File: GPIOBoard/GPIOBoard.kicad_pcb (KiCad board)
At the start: 2 copper layers, 70 x 45 mm, 85 parts, among them J1 GPIO1, J10 USB_C_Receptacle_USB2.0_16P, J11 SWD, J12 CAN, J2 GPIO2, J3 GPIO3, J4 GPIO4, J5 GPIO5, J6 GPIO6, J7 GPIO7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

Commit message: GPIO Board ver1.1
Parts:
- removed the REF** at (156.2, 99.9)
- added D17: CAN_R, LED_SMD:LED_0603_1608Metric, F.Cu at (132.2, 94.5)
- added R27: 420, Resistor_SMD:R_0603_1608Metric, F.Cu at (128.6, 94.5)
- added R28: 100, Resistor_SMD:R_0603_1608Metric, F.Cu at (162.5, 90.8)
- added R29: 600, Resistor_SMD:R_0603_1608Metric, F.Cu at (162.5, 92.5)
- added R30: 300, Resistor_SMD:R_0603_1608Metric, F.Cu at (162.5, 94.2)
- added R31: 10k, Resistor_SMD:R_0603_1608Metric, F.Cu at (142.7, 97.5)
- added REF**: Title, Anan-Robo_Footprint_Library:Title, F.Cu at (167.9, 113.6)
- added REF**: Info_M, Anan-Robo_Footprint_Library:Info_M, B.Cu at (156.2, 100.4)
- added U5: LED_GRB, LED_SMD:LED_ROHM_SMLVN6, F.Cu at (169.2, 106.0)
- C1, C2: value 10u -> 4.7u
- D11: value 3V3 -> PWR
- D12: value data -> Data
- D15, D16: footprint Diode_SMD:D_SOD-123 -> Diode_SMD:Nexperia_CFP3_SOD-123W
- J10: value USB_C_Receptacle_USB2.0_16P -> Debug
- R17, R18, R20, R23, R24: value 55 -> 96
- R19: value 150 -> 430
- SW3: footprint Anan-Robo_Footprint_Library:SSSS213202 -> Anan-Robo_Footprint_Library:SLW
- U2: value LM1117GS -> TLV1117-33
- moved D11 40.4 mm to (135.5, 108.8), turned to 0 degrees
- moved R19 37.1 mm to (135.5, 106.8), turned to 0 degrees
- moved C1 4.72 mm to (138.8, 104.2)
- moved C2 4.72 mm to (138.8, 101.0)
- moved SW3 4.08 mm to (134.5, 89.2)
- moved D16 3.50 mm to (122.8, 103.0)
- moved R25 3.27 mm to (134.6, 97.0)
- moved C12 3.25 mm to (135.2, 101.5)
- moved U2 3.18 mm to (144.5, 103.2)
- moved U4 3.17 mm to (130.5, 101.5)
- moved JP1 3.07 mm to (128.6, 97.0)
- moved F1 2.25 mm to (122.0, 101.8)
- moved Y1 1.64 mm to (153.4, 91.7)
- moved C10 1.23 mm to (157.1, 90.8)
- moved C9 1.23 mm to (157.1, 92.8)
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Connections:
- U1 pad 10: unconnected-(U1-PA4-Pad10) -> /MCU/LED_R
- U1 pad 18: unconnected-(U1-PA8-Pad18) -> /MCU/LED_G
- U1 pad 6: unconnected-(U1-PA0-Pad6) -> /MCU/LED_B
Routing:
- net /MCU/LED_G: track 0.00 -> 22.9 mm, vias 0 -> 2
- net /MCU/LED_R: track 0.00 -> 17.6 mm, vias 0 -> 2
- net Net-(R28-Pad1): track 0.00 -> 16.5 mm
- net Net-(R29-Pad1): track 0.00 -> 15.7 mm
- net Net-(R30-Pad1): track 0.00 -> 15.0 mm
- net /MCU/LED_B: track 0.00 -> 12.8 mm, vias 0 -> 2
- net /CAN/CAN_L: track 22.5 -> 32.1 mm
- net Net-(SW3B-B): track 0.00 -> 7.73 mm
- net /CAN/CAN_H: track 16.5 -> 22.0 mm
- net Net-(SW3A-B): track 7.46 -> 12.2 mm
- net Net-(U1-BOOT0): track 4.54 -> 8.51 mm
- net Net-(U1-PF0): track 5.82 -> 8.77 mm
- net +5V: track 76.4 -> 79.0 mm, vias 3 -> 4
- net Net-(J12-Pin_1): track 7.66 -> 5.50 mm
- net +3.3V: track 184.9 -> 182.9 mm
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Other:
- board text added: "GNDD"
- board text added: "MCU"
- board text added: "ver 1.1: 2025-04-12"
- board text removed: "GPIO Board"
- board text removed: "ver 1.0 by yuta"
- board text removed: "ver 1.0: 2025-03-10"

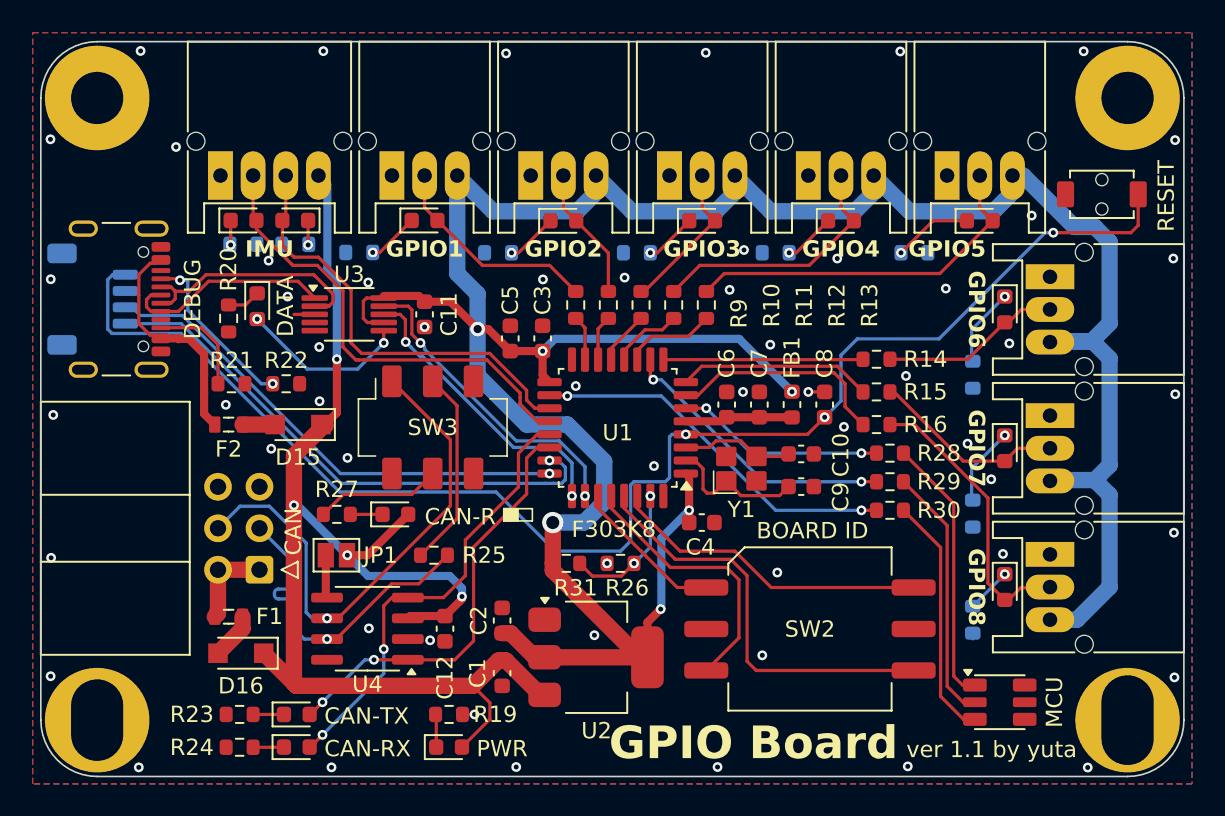
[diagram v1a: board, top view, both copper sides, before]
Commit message: GPIO Board ver1.2
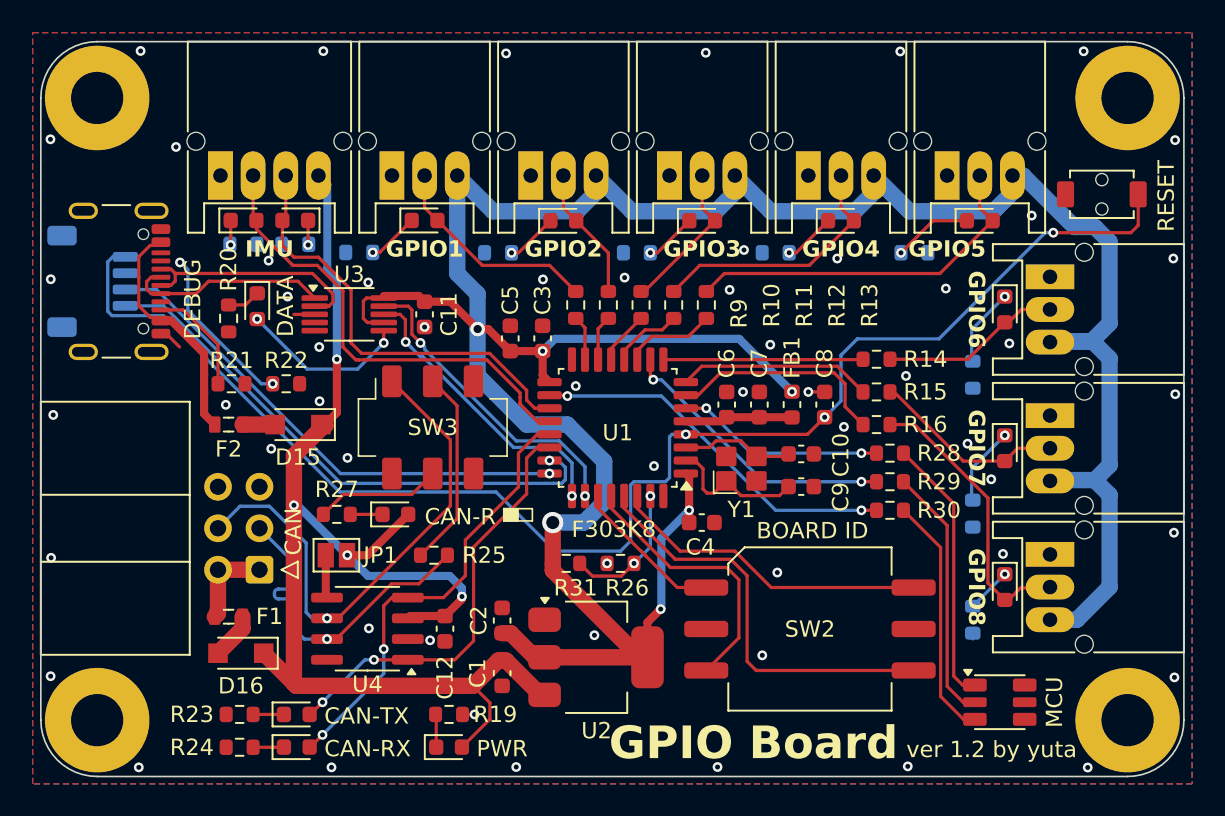
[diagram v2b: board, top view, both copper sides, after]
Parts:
- moved J10 1.09 mm to (114.2, 80.2)
- moved J11 1.09 mm to (113.7, 80.2)
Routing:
- net GNDD: track 3.11 -> 4.59 mm
- net Net-(F2-Pad2): track 14.5 -> 13.6 mm
- net Net-(J10-CC2): track 5.92 -> 6.77 mm
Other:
- board text added: "ver 1.2: 2025-07-01"
- board text removed: "ver 1.1: 2025-04-12"

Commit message: GPIO Board ver1.3
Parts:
- moved SW2 6.00 mm to (157.6, 101.5)
- moved SW1 2.50 mm to (175.5, 74.9)
- moved F1 1.00 mm to (122.0, 100.8)
- moved F2 1.00 mm to (122.0, 89.0)
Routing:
- net Net-(J10-CC1): track 10.3 -> 11.4 mm
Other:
- board text added: "ver 1.3: 2025-07-16"
- board text removed: "ver 1.2: 2025-07-01"
